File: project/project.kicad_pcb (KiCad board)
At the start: 2 copper layers, 85.5 x 86 mm, 318 parts, among them J1001 input_1x5, J101 FFC Connector, J201 input_1x5, J301 input_1x5, J401 input_1x5, J501 input_1x5, J601 input_1x5, J701 input_1x5, J801 input_1x5, Q1001 MMBTA44, Q1002 MMBTA44, Q1003 MMBTA44, Q1004 MMBTA44, Q1005 MMBTA44, Q1006 MMBTA44, Q1007 MMBTA44, Q1008 MMBTA44, Q201 MMBTA44, Q202 MMBTA44, Q203 MMBTA44, Q204 MMBTA44, Q205 MMBTA44, Q206 MMBTA44, Q207 MMBTA44, Q208 MMBTA44, Q301 MMBTA44, Q302 MMBTA44, Q303 MMBTA44, Q304 MMBTA44, Q305 MMBTA44, Q306 MMBTA44, Q307 MMBTA44, Q308 MMBTA44, Q401 MMBTA44, Q402 MMBTA44, Q403 MMBTA44, Q404 MMBTA44, Q405 MMBTA44, Q406 MMBTA44, Q407 MMBTA44, Q408 MMBTA44, Q501 MMBTA44, Q502 MMBTA44, Q503 MMBTA44, Q504 MMBTA44, Q505 MMBTA44, Q506 MMBTA44, Q507 MMBTA44, Q508 MMBTA44, Q601 MMBTA44, Q602 MMBTA44, Q603 MMBTA44, Q604 MMBTA44, Q605 MMBTA44, Q606 MMBTA44, Q607 MMBTA44, Q608 MMBTA44, Q701 MMBTA44, Q702 MMBTA44, Q703 MMBTA44, Q704 MMBTA44, Q705 MMBTA44, Q706 MMBTA44, Q707 MMBTA44, Q708 MMBTA44, Q801 MMBTA44, Q802 MMBTA44, Q803 MMBTA44, Q804 MMBTA44, Q805 MMBTA44, Q806 MMBTA44, Q807 MMBTA44, Q808 MMBTA44, U1001 LTV-244-GB-G, U101 74HC165, U102 74HC165, U103 GX101, U104 74HC165, U105 74HC165, U201 LTV-244-GB-G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

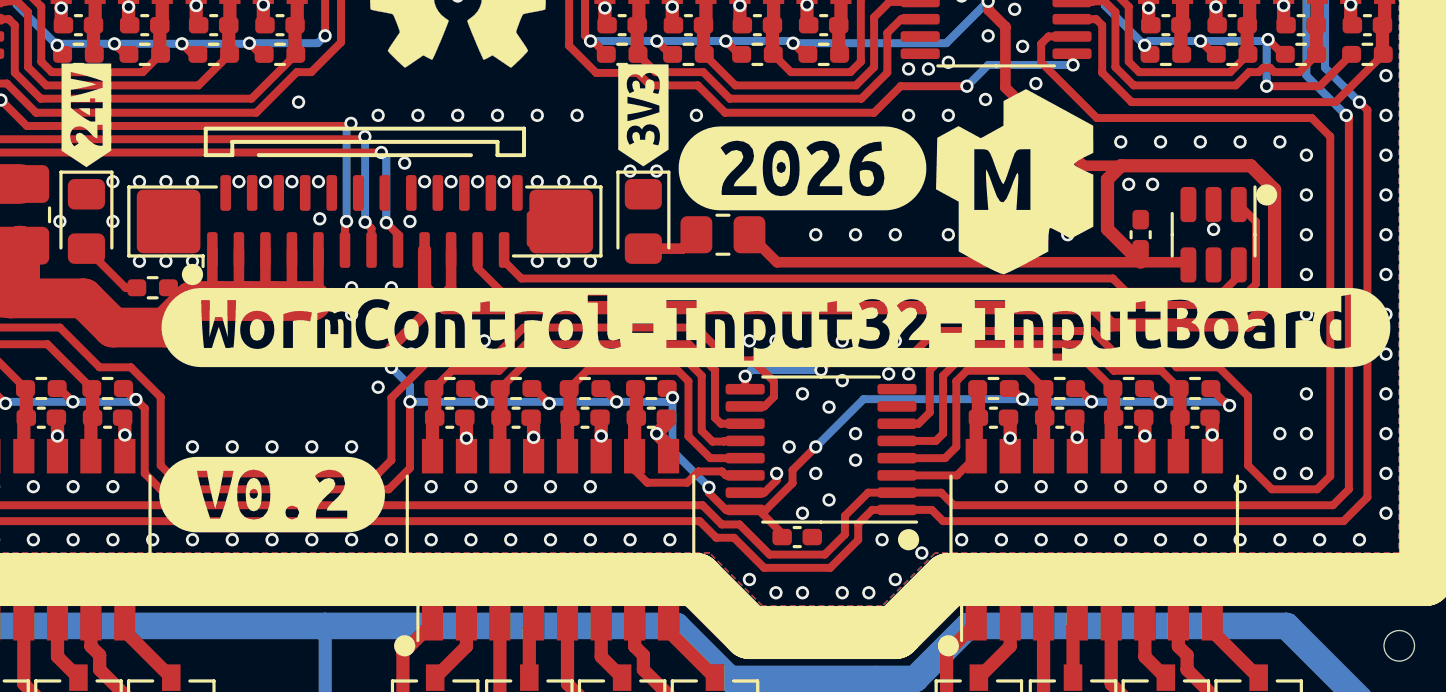
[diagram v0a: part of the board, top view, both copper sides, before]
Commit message: replacing thermometer
* Switching to TMP102 as TMP101 is no longer available
* bumping up version
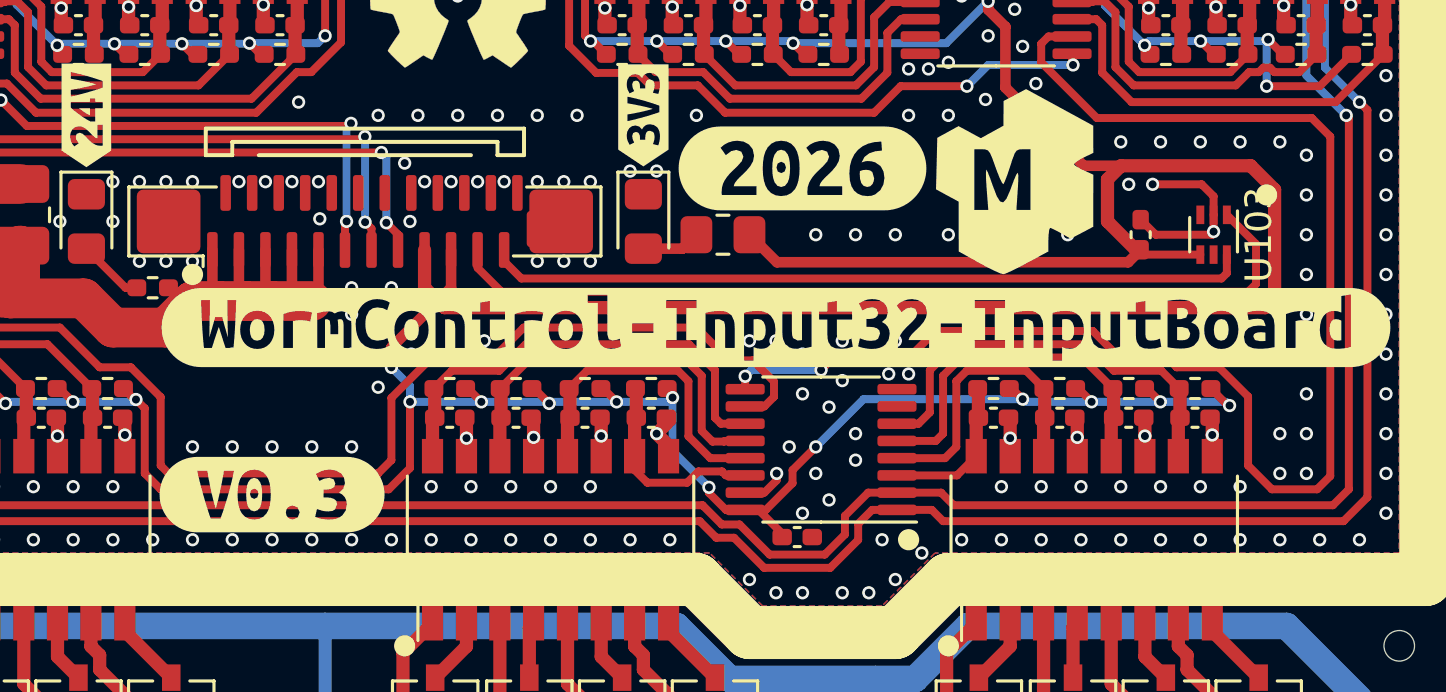
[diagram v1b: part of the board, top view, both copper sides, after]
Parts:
- removed kibuzzard-69735EB9: G***, kibuzzard-69735EB9
- added kibuzzard-69BC6B4D: G***, kibuzzard-69BC6B4D, F.Cu at (164.8, 101.3)
- U103: value GX101 -> TMP102; footprint Package_TO_SOT_SMD:SOT-23-6 -> -local:SOT-563
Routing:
- net GND: track 55.5 -> 62.4 mm
- net SCL: track 34.2 -> 33.6 mm
- net SDA: track 29.3 -> 28.7 mm

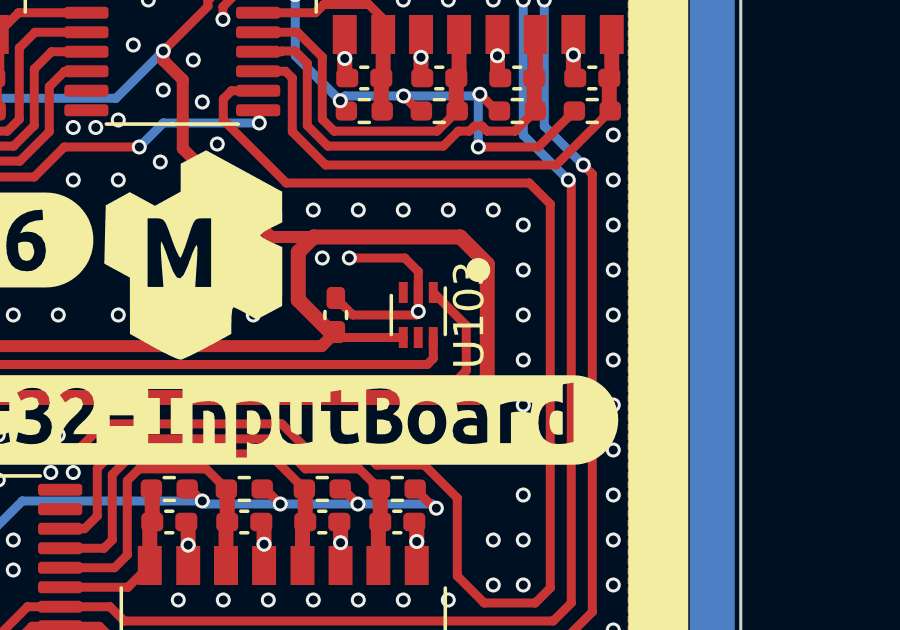
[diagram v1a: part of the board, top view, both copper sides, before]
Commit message: fixing tmp102 pinout
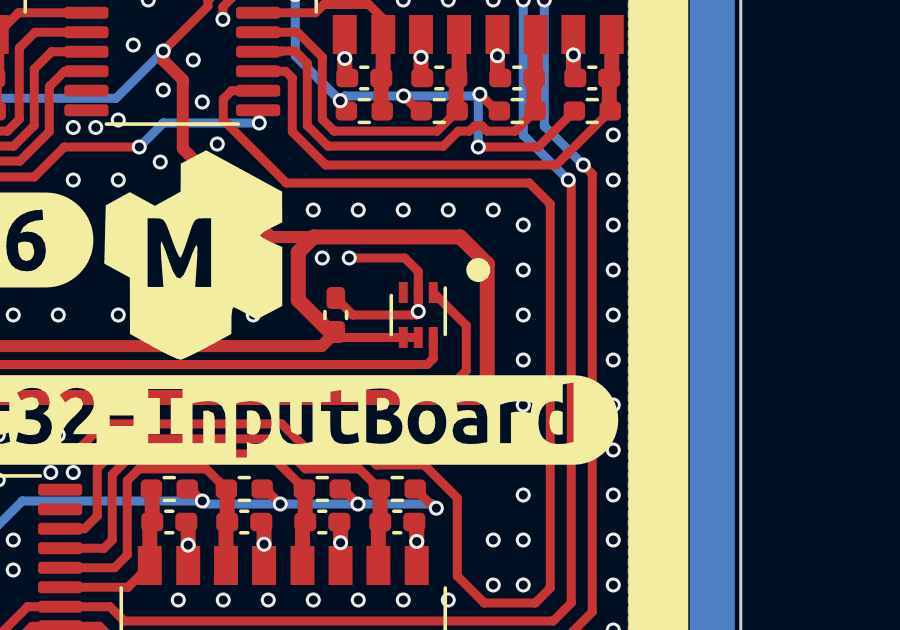
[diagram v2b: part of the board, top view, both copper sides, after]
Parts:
- renumbered C101 to C1, C301 to C10, C302 to C11, C303 to C12, C304 to C13, C401 to C14, C402 to C15, C403 to C16, C404 to C17, C501 to C18, C502 to C19, C102 to C2, C503 to C20, C504 to C21, C601 to C22, C602 to C23, C603 to C24, C604 to C25, C701 to C26, C702 to C27, C703 to C28, C704 to C29, C103 to C3, C801 to C30, C802 to C31, C803 to C32, C804 to C33, C901 to C34, C902 to C35, C903 to C36, C904 to C37, C905 to C38, C1001 to C39, C104 to C4, C1002 to C40, C1003 to C41, C1004 to C42, C105 to C5, C201 to C6, C202 to C7, C203 to C8, C204 to C9, D101 to D1, D401 to D10, D402 to D11, D403 to D12, D404 to D13, D501 to D14, D502 to D15, D503 to D16, D504 to D17, D601 to D18, D602 to D19, D201 to D2, D603 to D20, D604 to D21, D701 to D22, D702 to D23, D703 to D24, D704 to D25, D801 to D26, D802 to D27, D803 to D28, D804 to D29, D202 to D3, D901 to D30, D902 to D31, D1001 to D32, D1002 to D33, D1003 to D34, D1004 to D35, D203 to D4, D204 to D5, D301 to D6, D302 to D7, D303 to D8, D304 to D9, F201 to F1, F301 to F2, F401 to F3, F501 to F4, F601 to F5, F701 to F6, F801 to F7, F1001 to F8, G101 to G1, G102 to G2, J101 to J1, J201 to J2, J301 to J3, J401 to J4, J501 to J5, J601 to J6, J701 to J7, J801 to J8, J1001 to J9, L901 to L1, L902 to L2, PS901 to PS1, Q201 to Q1, Q302 to Q10, Q303 to Q11, Q304 to Q12, Q305 to Q13, Q306 to Q14, Q307 to Q15, Q308 to Q16, Q401 to Q17, Q402 to Q18, Q403 to Q19, Q202 to Q2, Q404 to Q20, Q405 to Q21, Q406 to Q22, Q407 to Q23, Q408 to Q24, Q501 to Q25, Q502 to Q26, Q503 to Q27, Q504 to Q28, Q505 to Q29, Q203 to Q3, Q506 to Q30, Q507 to Q31, Q508 to Q32, Q601 to Q33, Q602 to Q34, Q603 to Q35, Q604 to Q36, Q605 to Q37, Q606 to Q38, Q607 to Q39, Q204 to Q4, Q608 to Q40, Q701 to Q41, Q702 to Q42, Q703 to Q43, Q704 to Q44, Q705 to Q45, Q706 to Q46, Q707 to Q47, Q708 to Q48, Q801 to Q49, Q205 to Q5, Q802 to Q50, Q803 to Q51, Q804 to Q52, Q805 to Q53, Q806 to Q54, Q807 to Q55, Q808 to Q56, Q1001 to Q57, Q1002 to Q58, Q1003 to Q59, Q206 to Q6, Q1004 to Q60, Q1005 to Q61, Q1006 to Q62, Q1007 to Q63, Q1008 to Q64, Q207 to Q7, Q208 to Q8, Q301 to Q9, R101 to R1, R209 to R10, R803 to R100, R804 to R101, R805 to R102, R806 to R103, R807 to R104, R808 to R105, R809 to R106, R810 to R107, R811 to R108, R812 to R109, R210 to R11, R813 to R110, R814 to R111, R815 to R112, R816 to R113, R901 to R114, R902 to R115, R903 to R116, R1001 to R117, R1002 to R118, R1003 to R119, R211 to R12, R1004 to R120, R1005 to R121, R1006 to R122, R1007 to R123, R1008 to R124, R1009 to R125, R1010 to R126, R1011 to R127, R1012 to R128, R1013 to R129, R212 to R13, R1014 to R130, R1015 to R131, R1016 to R132, R213 to R14, R214 to R15, R215 to R16, R216 to R17, R301 to R18, R302 to R19, R201 to R2, R303 to R20, R304 to R21, R305 to R22, R306 to R23, R307 to R24, R308 to R25, R309 to R26, R310 to R27, R311 to R28, R312 to R29, R202 to R3, R313 to R30, R314 to R31, R315 to R32, R316 to R33, R401 to R34, R402 to R35, R403 to R36, R404 to R37, R405 to R38, R406 to R39, R203 to R4, R407 to R40, R408 to R41, R409 to R42, R410 to R43, R411 to R44, R412 to R45, R413 to R46, R414 to R47, R415 to R48, R416 to R49, R204 to R5, R501 to R50, R502 to R51, R503 to R52, R504 to R53, R505 to R54, R506 to R55, R507 to R56, R508 to R57, R509 to R58, R510 to R59, R205 to R6, R511 to R60, R512 to R61, R513 to R62, R514 to R63, R515 to R64, R516 to R65, R601 to R66, R602 to R67, R603 to R68, R604 to R69, R206 to R7, R605 to R70, R606 to R71, R607 to R72, R608 to R73, R609 to R74, R610 to R75, R611 to R76, R612 to R77, R613 to R78, R614 to R79, R207 to R8, R615 to R80, R616 to R81, R701 to R82, R702 to R83, R703 to R84, R704 to R85, R705 to R86, R706 to R87, R707 to R88, R708 to R89, R208 to R9, R709 to R90, R710 to R91, R711 to R92, R712 to R93, R713 to R94, R714 to R95, R715 to R96, R716 to R97, R801 to R98, R802 to R99, U101 to U1, U601 to U10, U701 to U11, U801 to U12, U1001 to U13, U102 to U2, U103 to U3, U104 to U4, U105 to U5, U201 to U6, U301 to U7, U401 to U8, U501 to U9
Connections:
- U3 pad 5: unconnected-(U103-Pad5) -> +3V3
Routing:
- net +3V3: track 284.3 -> 284.8 mm
